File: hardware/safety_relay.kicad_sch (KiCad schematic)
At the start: 5 parts, among them K1 FINDER-30.22, Q1 BSS138

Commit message: Refactor
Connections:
- net SAFETY1 renamed OUT
- net SAFETY2 renamed IN
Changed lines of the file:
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@@
     (effects (font (size 1.27 1.27)) (justify right))
   )
-  (hierarchical_label "SAFETY2" (shape input) (at 153.67 100.33 270) (fields_autoplaced)
+  (hierarchical_label "IN" (shape input) (at 153.67 100.33 270) (fields_autoplaced)
     (effects (font (size 1.27 1.27)) (justify right))
   )
-  (hierarchical_label "SAFETY1" (shape output) (at 156.21 82.55 90) (fields_autoplaced)
+  (hierarchical_label "OUT" (shape output) (at 156.21 82.55 90) (fields_autoplaced)
     (effects (font (size 1.27 1.27)) (justify left))
   )
@@
     (pin "A2")
     (instances
-      (project "APPS"
+      (project "apps"
         (path "/fc4ad874-c922-4070-89f9-7262080469d8/00000000-0000-0000-0000-00005f99e99e"
           (reference "K1") (unit 1)
@@
     (pin "2")
     (instances
-      (project "APPS"
+      (project "apps"
         (path "/fc4ad874-c922-4070-89f9-7262080469d8/00000000-0000-0000-0000-00005f99e99e"
           (reference "D8") (unit 1)
@@
     (pin "3")
     (instances
-      (project "APPS"
+      (project "apps"
         (path "/fc4ad874-c922-4070-89f9-7262080469d8/00000000-0000-0000-0000-00005f99e99e"
           (reference "Q1") (unit 1)
@@
     (pin "2")
     (instances
-      (project "APPS"
+      (project "apps"
         (path "/fc4ad874-c922-4070-89f9-7262080469d8/00000000-0000-0000-0000-00005f99e99e"
           (reference "R34") (unit 1)
@@
     (pin "2")
     (instances
-      (project "APPS"
+      (project "apps"
         (path "/fc4ad874-c922-4070-89f9-7262080469d8/00000000-0000-0000-0000-00005f99e99e"
           (reference "R35") (unit 1)
@@
     (pin "1")
     (instances
-      (project "APPS"
+      (project "apps"
         (path "/fc4ad874-c922-4070-89f9-7262080469d8/00000000-0000-0000-0000-00005f99e99e"
           (reference "#PWR055") (unit 1)
@@
     (pin "1")
     (instances
-      (project "APPS"
+      (project "apps"
         (path "/fc4ad874-c922-4070-89f9-7262080469d8/00000000-0000-0000-0000-00005f99e99e"
           (reference "#PWR056") (unit 1)

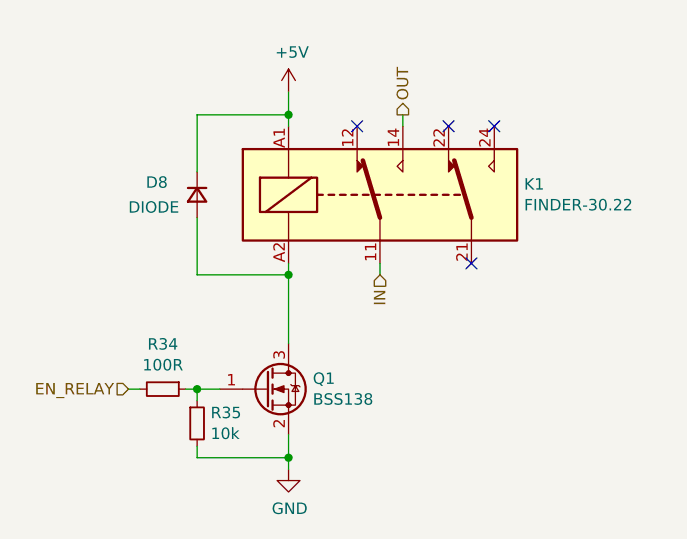
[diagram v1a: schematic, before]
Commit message: Update component values
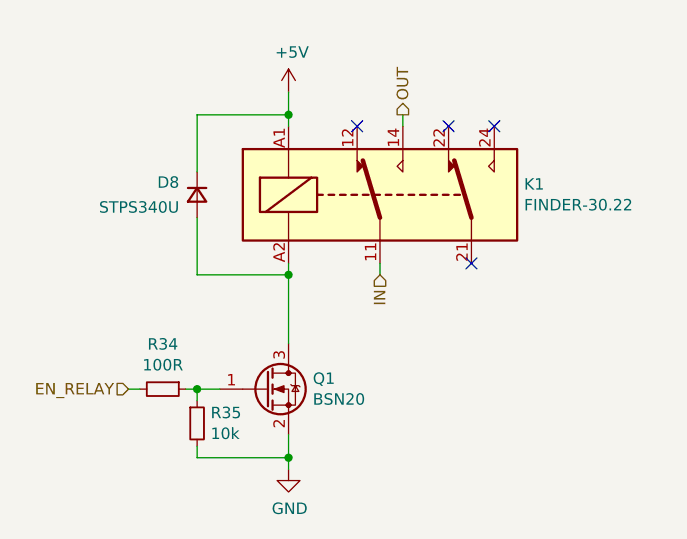
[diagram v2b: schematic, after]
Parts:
- D8: value DIODE -> STPS340U
- Q1: value BSS138 -> BSN20
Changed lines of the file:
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@@
   (symbol (lib_id "Device:D_Small") (at 133.35 91.44 270) (unit 1)
     (in_bom yes) (on_board yes) (dnp no)
-    (property "Reference" "D8" (at 130.0988 90.0684 90)
+    (property "Reference" "D8" (at 131.3688 90.0684 90)
       (effects (font (size 1.27 1.27)) (justify right))
     )
-    (property "Value" "DIODE" (at 131.3688 92.837 90)
+    (property "Value" "STPS340U" (at 131.3688 92.837 90)
       (effects (font (size 1.27 1.27)) (justify right))
     )
@@
       (effects (font (size 1.27 1.27)) (justify left))
     )
-    (property "Value" "BSS138" (at 146.2024 114.173 0)
+    (property "Value" "BSN20" (at 146.2024 114.173 0)
       (effects (font (size 1.27 1.27)) (justify left))
     )
